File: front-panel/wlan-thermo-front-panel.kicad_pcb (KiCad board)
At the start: 2 copper layers, 60.9 x 43.5 mm, 26 parts, among them IC1 ME6211C33M5G-N, J1 PROG_HDR, J2 Conn_01x02, J3 Conn_01x02, Q1 UMH3N, SW1 SW_Push, SW2 RotaryEncoder_Switch, U1 ESP-12F, U2 SHT4x, U3 SSD1306

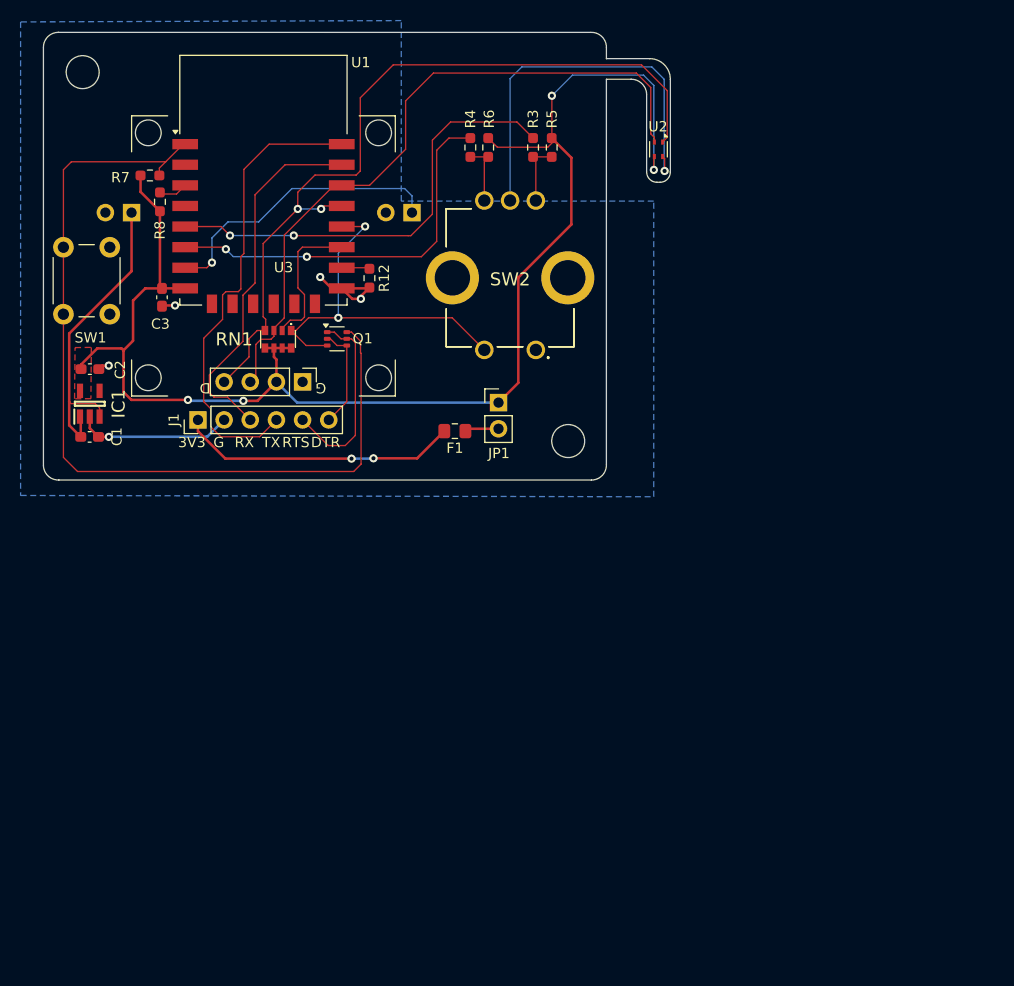
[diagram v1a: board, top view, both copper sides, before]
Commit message: crc checked first version of board with backend shelly
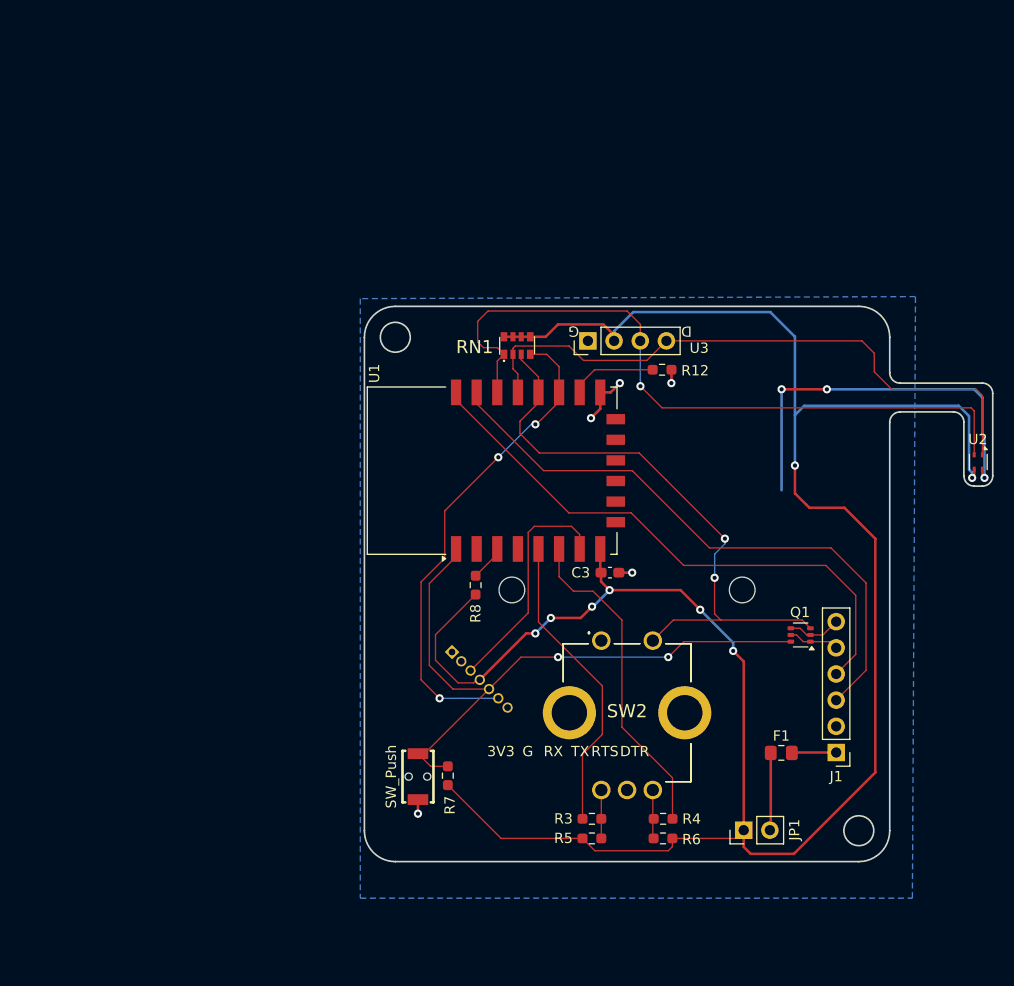
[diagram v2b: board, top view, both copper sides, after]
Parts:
- removed C1, C2: 1uF, Capacitor_SMD:C_0603_1608Metric_Pad1.08x0.95mm_HandSolder
- removed H1, H2: MountingHole, MountingHole:MountingHole_3.2mm_M3
- removed IC1: ME6211C33M5G-N, Chof747 Footprints:SOT95P270X145-5N
- removed J3: Conn_01x02, Connector_PinHeader_2.54mm:PinHeader_1x02_P2.54mm_Vertical
- J2: value Conn_01x02 -> Device Connector; footprint Connector_PinHeader_2.54mm:PinHeader_1x02_P2.54mm_Vertical -> Connector_PinHeader_1.27mm:PinHeader_1x07_P1.27mm_Vertical
- SW1: footprint Button_Switch_THT:SW_PUSH_6mm -> Chof747 Footprints:KEY-SMD_L3.9-W3.0-LS5.0-EH
- moved J1 69.9 mm to (174.3, 106.4), turned to 180 degrees
- moved R6 69.2 mm to (157.5, 114.7), turned to 0 degrees
- moved R4 67.8 mm to (157.5, 112.8), turned to 180 degrees
- moved R5 67.2 mm to (150.6, 114.7), turned to 180 degrees
- moved R3 65.4 mm to (150.6, 112.8), turned to 0 degrees
- moved R7 65.1 mm to (136.6, 108.6), turned to 90 degrees
- moved G*** 64.6 mm to (170.3, 87.9)
- moved SW1 56.6 mm to (133.7, 108.7), turned to -90 degrees
- moved Q1 53.4 mm to (170.8, 95.0), turned to 180 degrees
- moved J2 52.8 mm to (137.0, 96.6), turned to -135 degrees
- moved C3 51.0 mm to (152.3, 88.9), turned to 0 degrees
- moved R8 48.2 mm to (139.3, 90.1)
- moved JP1 47.9 mm to (165.3, 113.9), turned to 90 degrees
- moved F1 44.5 mm to (169.0, 106.4), turned to 0 degrees
- moved U2 43.4 mm to (188.1, 78.2)
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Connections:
- J2 pad 1: +5V -> unconnected-(J2-Pin_1-Pad1)
- J2 pad 2: GND -> unconnected-(J2-Pin_2-Pad2)
- RN1 pad 1: ~{GPIO0_RENBTN_FLASH} -> GPIO5_SCL
- RN1 pad 2: GPIO2 -> GPIO4_SDA
- RN1 pad 3: GPIO5_SCL -> ~{GPIO0_RENBTN_FLASH}
- RN1 pad 4: GPIO4_SDA -> GPIO2_RELAY
- U1 pad 17: GPIO2 -> GPIO2_RELAY
- U1 pad 7: GPIO13_RELAY -> GPIO13_RX1
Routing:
- net +3V3: track 137.3 -> 222.0 mm, vias 4 -> 8
- net GPIO2_RELAY: track 0.00 -> 47.8 mm, vias 0 -> 3
- net +5V: track 30.8 -> 0.00 mm
- net GPIO13_RELAY: track 28.5 -> 0.00 mm, vias 1 -> 0
- net GPIO3_RX: track 35.7 -> 58.7 mm
- net /3v3PROG: track 27.2 -> 4.32 mm, vias 2 -> 0
- net GPIO13_RX1: track 0.00 -> 22.7 mm
- net ~{RESET}: track 85.8 -> 63.2 mm, vias 0 -> 2
- net ~{GPIO0_RENBTN_FLASH}: track 36.9 -> 58.3 mm
- net GPIO4_SDA: track 77.8 -> 60.5 mm, vias 2 -> 0
- net GND: track 64.8 -> 47.6 mm, vias 6 -> 8
- net GPIO14_RENCLK: track 43.6 -> 29.6 mm, vias 2 -> 0
- net GPIO2: track 13.9 -> 0.00 mm
- net RTS: track 18.7 -> 4.92 mm
- net GPIO4_TX: track 45.6 -> 55.8 mm
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- removed copper zone on F.Cu, net +3V3
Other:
- board size 60.9 x 43.5 mm -> 61 x 53.9 mm
- board text removed: "5V"
- board text removed: "GND"
- board text removed: "REL"

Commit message: minor changes
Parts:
- added JP2: Wake, Jumper:SolderJumper-2_P1.3mm_Open_Pad1.0x1.5mm, F.Cu at (131.2, 93.5)
- moved J2 0.42 mm to (137.3, 96.3)
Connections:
- U1 pad 4: unconnected-(U1-GPIO16-Pad4) -> GPIO16_WAKE
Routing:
- net GPIO16_WAKE: track 0.00 -> 15.4 mm, vias 0 -> 2
- net ~{RESET}: track 63.2 -> 69.5 mm, vias 2 -> 4

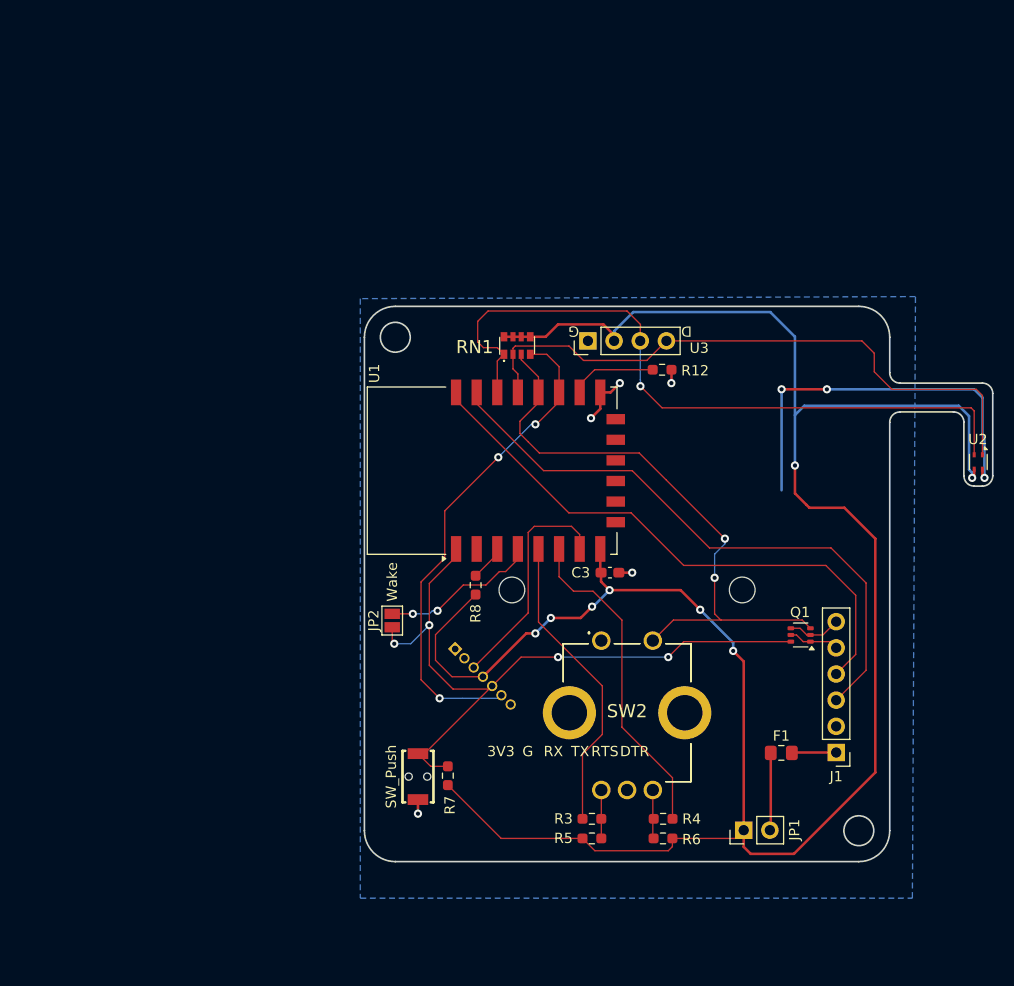
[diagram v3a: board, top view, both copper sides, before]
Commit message: Changed position of temp sensor
Moved temp sensor to the bottom
Replaced and rerouted other components
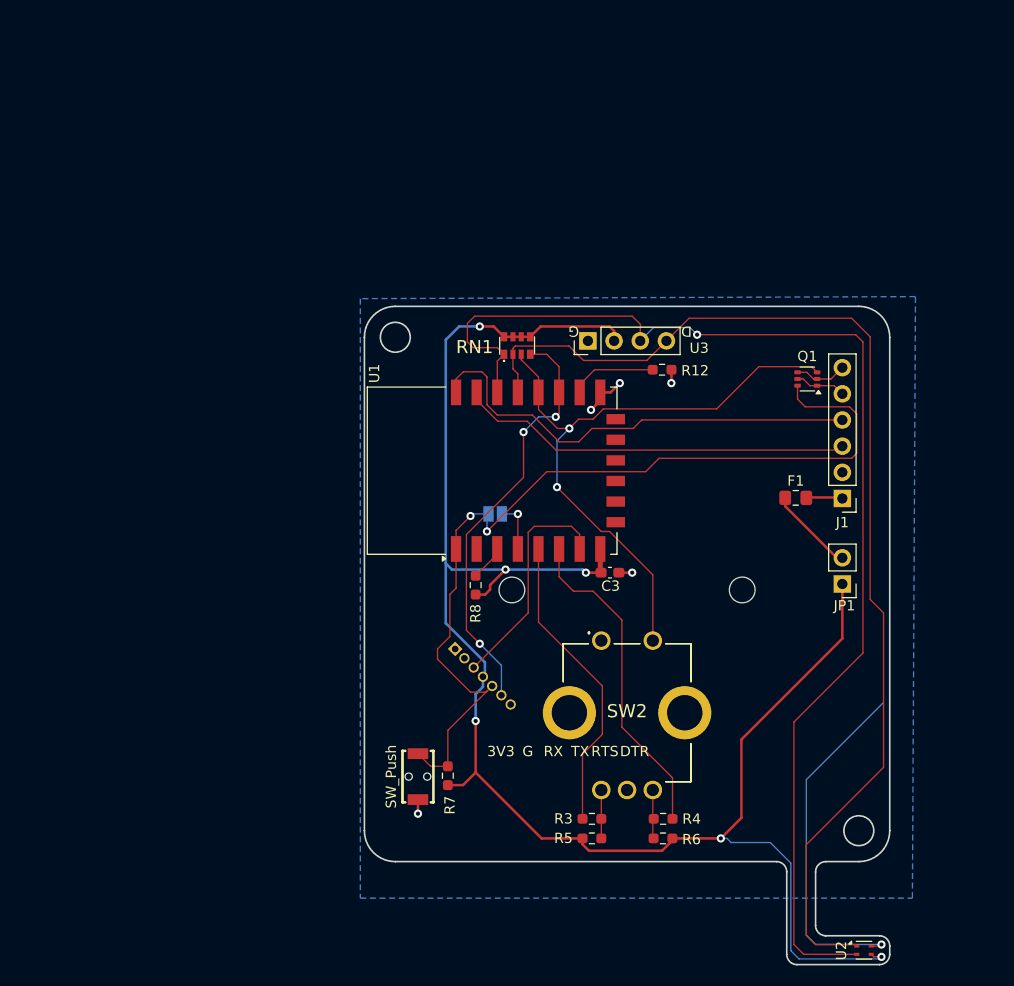
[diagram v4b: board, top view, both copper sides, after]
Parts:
- JP2: moved to B.Cu
- moved U2 48.7 mm to (177.0, 125.6), turned to 0 degrees
- moved JP1 25.7 mm to (174.9, 90.0), turned to 180 degrees
- moved Q1 24.9 mm to (171.5, 70.1)
- moved F1 24.8 mm to (170.4, 81.6)
- moved J1 24.7 mm to (174.9, 81.7)
- moved JP2 14.4 mm to (141.2, 83.2), turned to 0 degrees
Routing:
- net GPIO5_SCL: track 69.4 -> 119.4 mm
- net +3V3: track 221.5 -> 172.0 mm, vias 8 -> 6
- net GPIO4_SDA: track 60.5 -> 109.3 mm
- net GPIO3_RX: track 58.7 -> 38.6 mm
- net ~{RESET}: track 69.5 -> 88.5 mm, vias 4 -> 2
- net GPIO4_TX: track 55.8 -> 44.4 mm
- net GPIO16_WAKE: track 15.4 -> 4.95 mm, vias 2 -> 1
- net GPIO2_RELAY: track 47.8 -> 41.3 mm
- net GND: track 47.6 -> 42.8 mm, vias 8 -> 6
- net ~{GPIO0_RENBTN_FLASH}: track 58.3 -> 62.0 mm
- net /3v3PROG_SAVE: track 7.54 -> 8.44 mm
- net /3v3PROG: track 4.32 -> 3.56 mm
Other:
- board size 61 x 53.9 mm -> 51 x 63.9 mm
